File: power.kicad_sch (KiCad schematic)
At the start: 2 parts

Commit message: Updated power rails
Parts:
- added R39, R40: 0Ω, Resistor_SMD:R_0201_0603Metric, symbol Device:R_Small
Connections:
- new net +3.3V: R39.2
- new net +3.3VA: R40.2
- new net +3.3V_SYS: R39.1, R40.1

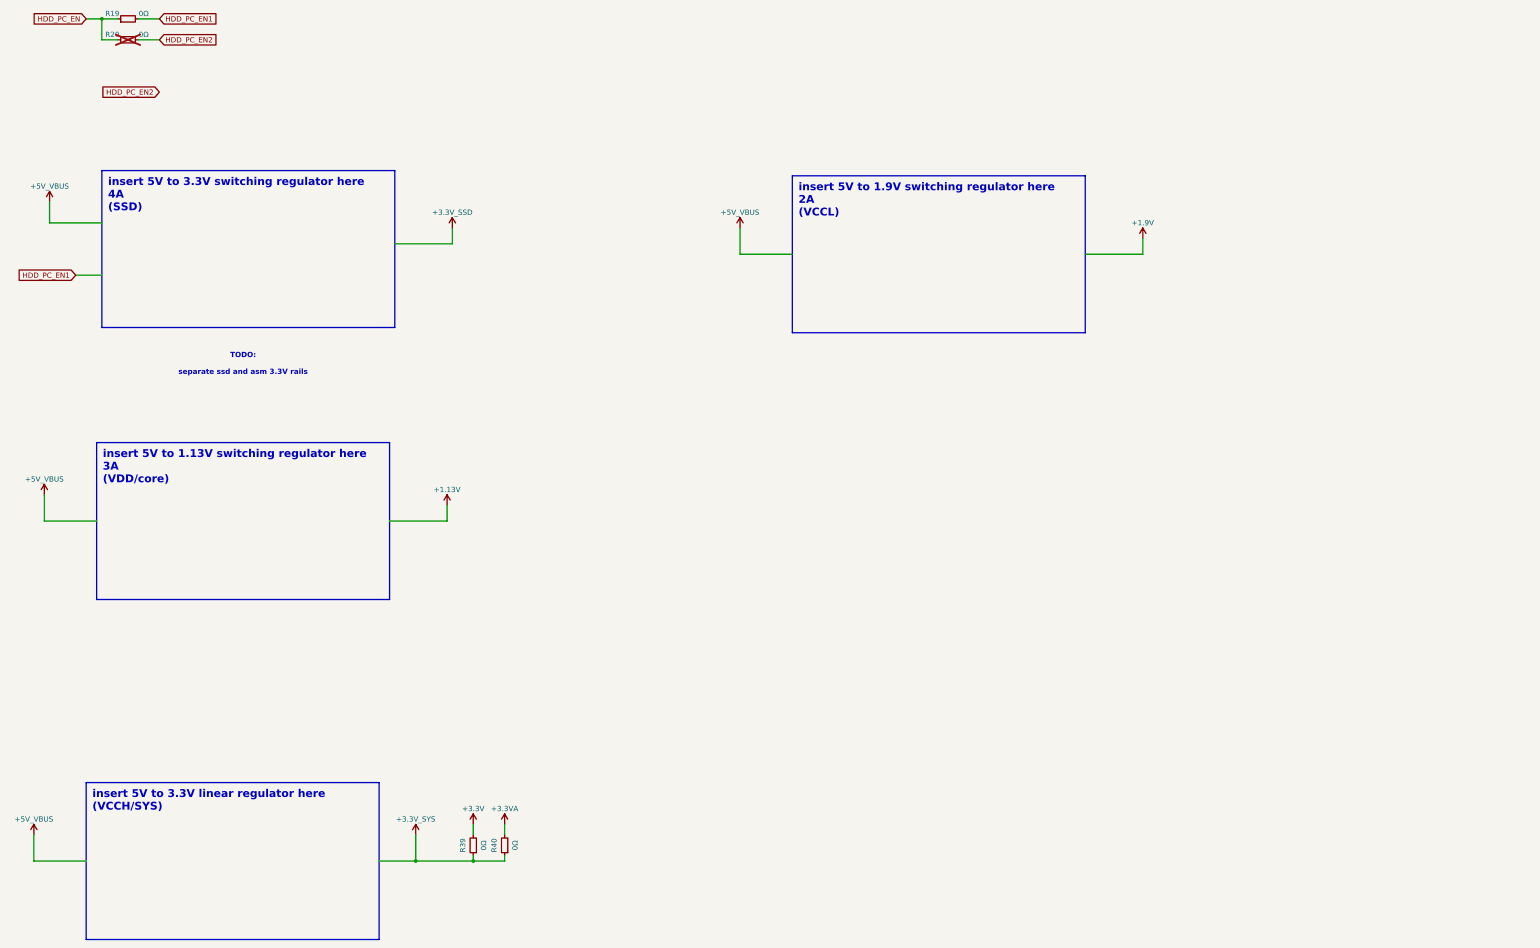
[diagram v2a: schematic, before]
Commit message: Changing from M.2 adapter to PCIe x4 adapter
I don't actually want an ssd enclosure, I want a PCIe-slot-giver for my laptop
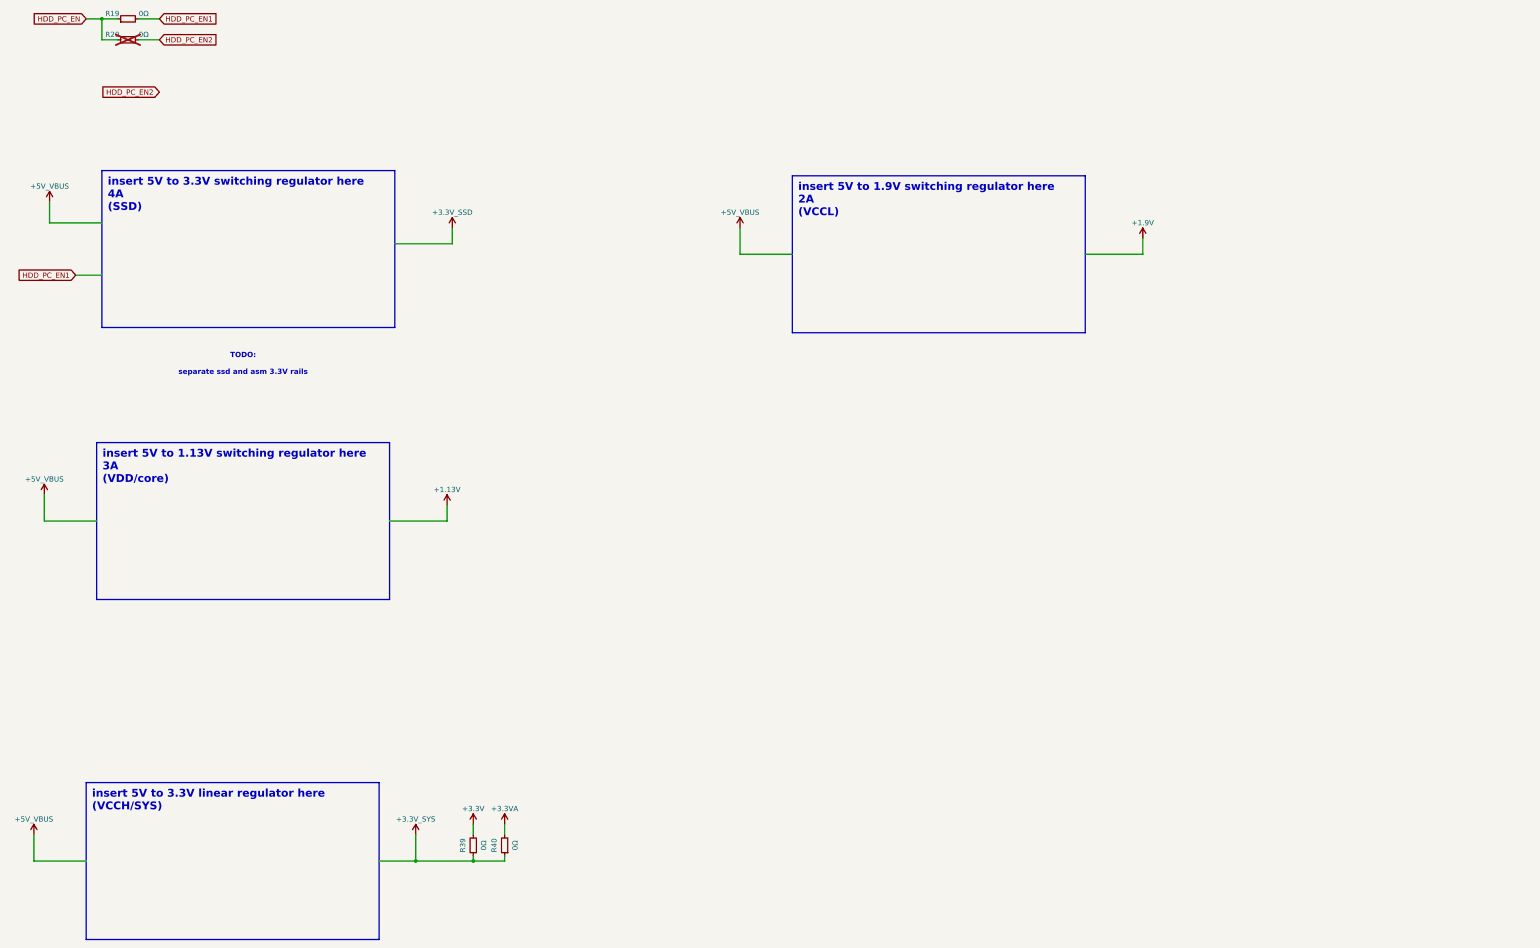
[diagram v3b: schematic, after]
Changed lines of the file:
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@@
 (kicad_sch
-	(version 20231120)
+	(version 20250114)
 	(generator "eeschema")
-	(generator_version "8.0")
+	(generator_version "9.0")
 	(paper "A3")
+	(text "TODO:\n\nseparate ssd and asm 3.3V rails"
+		(exclude_from_sim no)
+		(at 74.93 104.14 0)
+		(effects
+			(font
+				(size 1.27 1.27)
+				(thickness 0.254)
+				(bold yes)
+			)
+		)
+	)
+	(text_box "insert 5V to 1.13V switching regulator here\n3A\n(VDD/core)"
+		(exclude_from_sim no)
+		(at 39.37 123.19 0)
+		(size 71.12 38.1)
+		(margins 1.4288 1.4288 1.4288 1.4288)
+		(stroke
+			(width 0)
+			(type default)
+		)
+		(fill
+			(type none)
+		)
+		(effects
+			(font
+				(size 1.905 1.905)
+				(thickness 0.381)
+				(bold yes)
+			)
+			(justify left top)
+		)
+	)
+	(text_box "insert 5V to 1.9V switching regulator here\n2A\n(VCCL)"
+		(exclude_from_sim no)
+		(at 208.28 58.42 0)
+		(size 71.12 38.1)
+		(margins 1.4288 1.4288 1.4288 1.4288)
+		(stroke
+			(width 0)
+			(type default)
+		)
+		(fill
+			(type none)
+		)
+		(effects
+			(font
+				(size 1.905 1.905)
+				(thickness 0.381)
+				(bold yes)
+			)
+			(justify left top)
+		)
+	)
+	(text_box "insert 5V to 3.3V switching regulator here\n4A\n(SSD)\n"
+		(exclude_from_sim no)
+		(at 40.64 57.15 0)
+		(size 71.12 38.1)
+		(margins 1.4288 1.4288 1.4288 1.4288)
+		(stroke
+			(width 0)
+			(type default)
+		)
+		(fill
+			(type none)
+		)
+		(effects
+			(font
+				(size 1.905 1.905)
+				(thickness 0.381)
+				(bold yes)
+			)
+			(justify left top)
+		)
+	)
+	(text_box "insert 5V to 3.3V linear regulator here\n(VCCH/SYS)"
+		(exclude_from_sim no)
+		(at 36.83 205.74 0)
+		(size 71.12 38.1)
+		(margins 1.4288 1.4288 1.4288 1.4288)
+		(stroke
+			(width 0)
+			(type default)
+		)
+		(fill
+			(type none)
+		)
+		(effects
+			(font
+				(size 1.905 1.905)
+				(thickness 0.381)
+				(bold yes)
+			)
+			(justify left top)
+		)
+	)
 	(junction
 		(at 40.64 20.32)
@@
 		)
 	)
-	(text_box "insert 5V to 1.13V switching regulator here\n3A\n(VDD/core)"
-		(exclude_from_sim no)
-		(at 39.37 123.19 0)
-		(size 71.12 38.1)
-		(stroke
-			(width 0)
-			(type default)
-		)
-		(fill
-			(type none)
-		)
-		(effects
-			(font
-				(size 1.905 1.905)
-				(thickness 0.381)
-				(bold yes)
-			)
-			(justify left top)
-		)
-	)
-	(text_box "insert 5V to 1.9V switching regulator here\n2A\n(VCCL)"
-		(exclude_from_sim no)
-		(at 208.28 58.42 0)
-		(size 71.12 38.1)
-		(stroke
-			(width 0)
-			(type default)
-		)
-		(fill
-			(type none)
-		)
-		(effects
-			(font
-				(size 1.905 1.905)
-				(thickness 0.381)
-				(bold yes)
-			)
-			(justify left top)
-		)
-	)
-	(text_box "insert 5V to 3.3V switching regulator here\n4A\n(SSD)\n"
-		(exclude_from_sim no)
-		(at 40.64 57.15 0)
-		(size 71.12 38.1)
-		(stroke
-			(width 0)
-			(type default)
-		)
-		(fill
-			(type none)
-		)
-		(effects
-			(font
-				(size 1.905 1.905)
-				(thickness 0.381)
-				(bold yes)
-			)
-			(justify left top)
-		)
-	)
-	(text_box "insert 5V to 3.3V linear regulator here\n(VCCH/SYS)"
-		(exclude_from_sim no)
-		(at 36.83 205.74 0)
-		(size 71.12 38.1)
-		(stroke
-			(width 0)
-			(type default)
-		)
-		(fill
-			(type none)
-		)
-		(effects
-			(font
-				(size 1.905 1.905)
-				(thickness 0.381)
-				(bold yes)
-			)
-			(justify left top)
-		)
-	)
-	(text "TODO:\n\nseparate ssd and asm 3.3V rails"
-		(exclude_from_sim no)
-		(at 74.93 104.14 0)
-		(effects
-			(font
-				(size 1.27 1.27)
-				(thickness 0.254)
-				(bold yes)
-			)
-		)
-	)

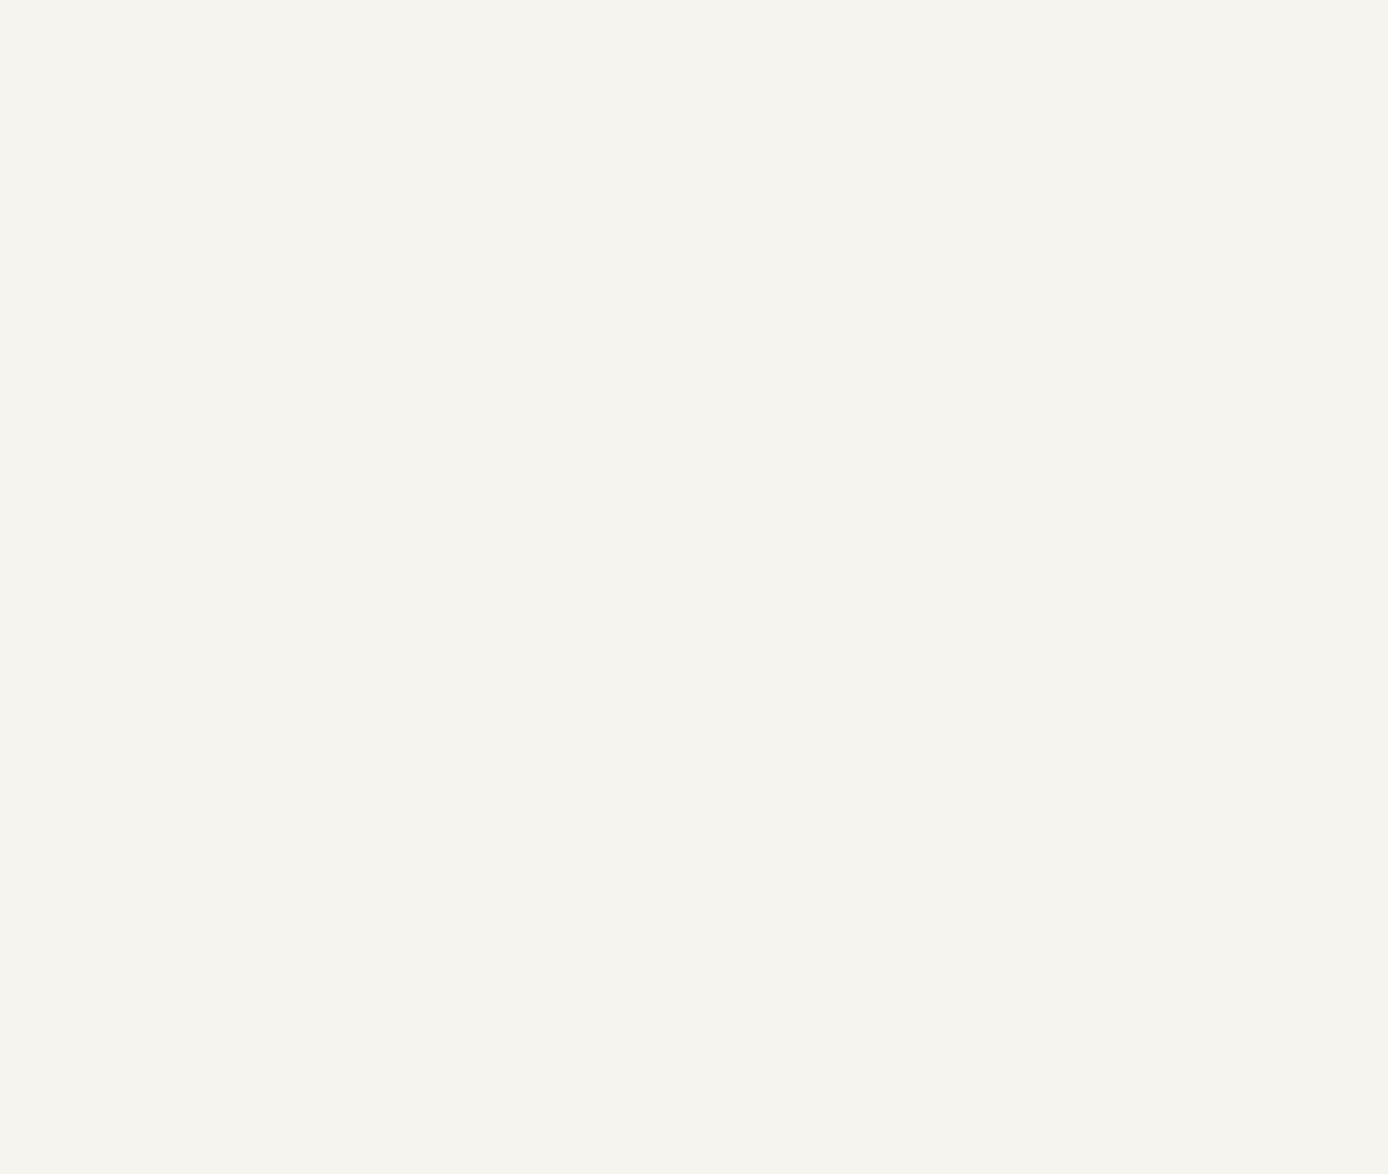
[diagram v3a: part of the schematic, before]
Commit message: Cleaning up schematic a bit
Directly copying the reference schematic was stupid lol, what a mess
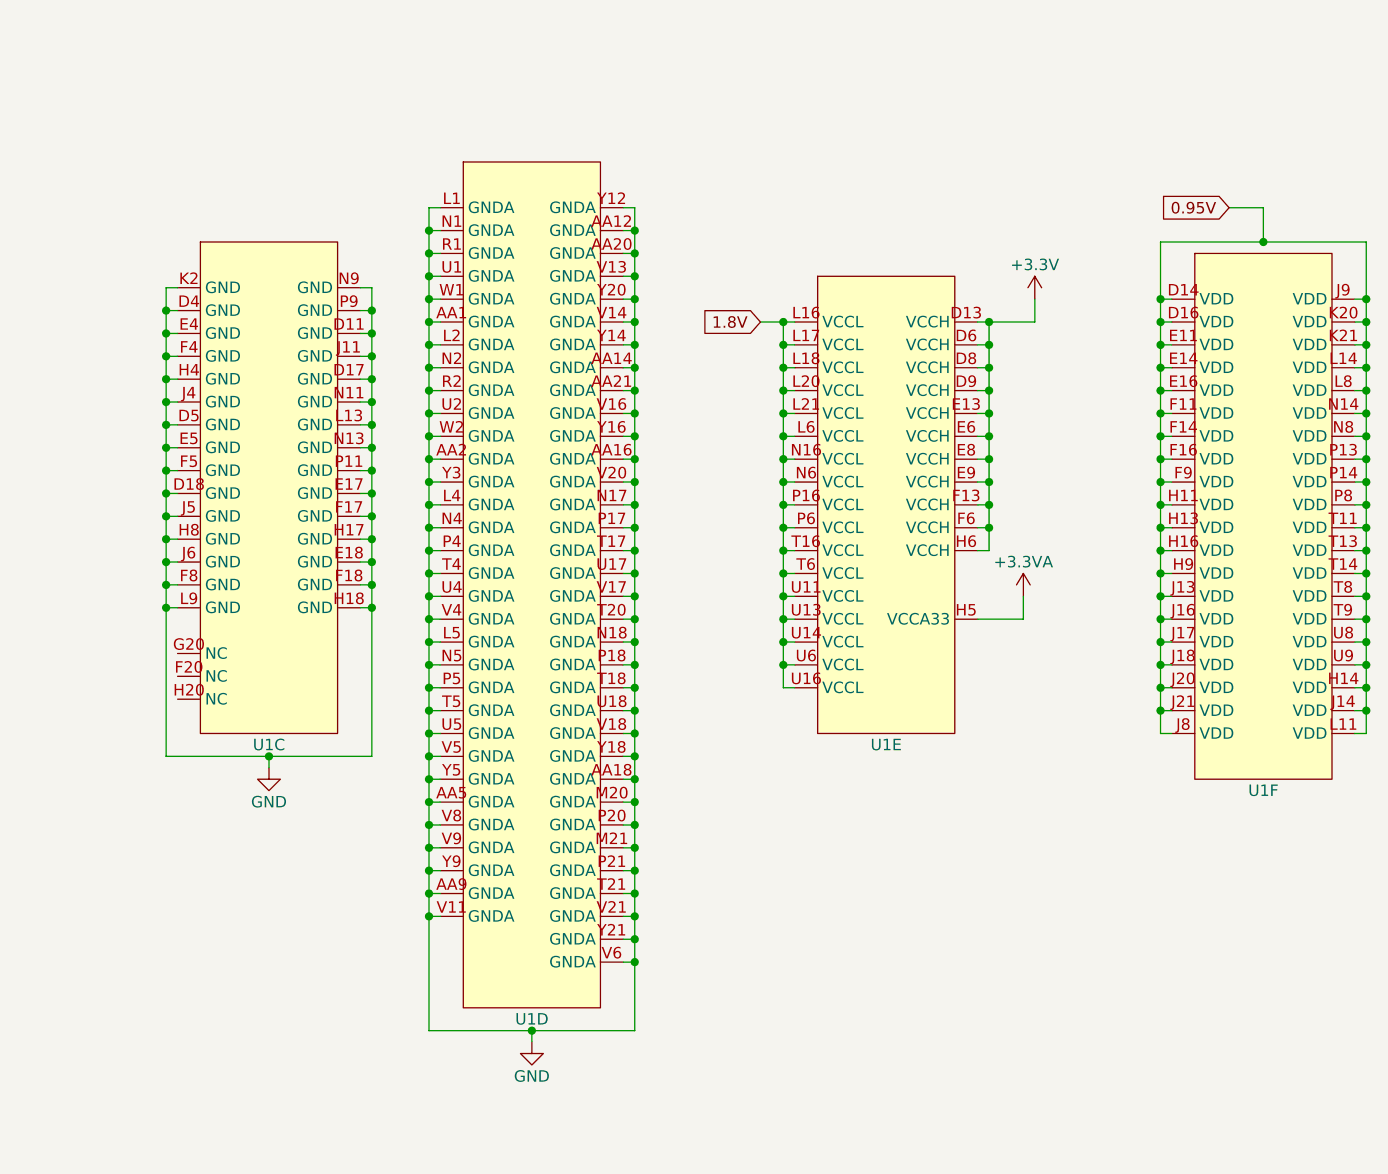
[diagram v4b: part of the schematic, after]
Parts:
- added U1: ~, A-my-stuff:ASM2464PD, symbol A_my_stuff:ASM2464PD
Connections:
- net +3.3V: now also U1.D13 (VCCH), U1.D6 (VCCH), U1.D8 (VCCH), U1.D9 (VCCH), U1.E13 (VCCH), U1.E6 (VCCH), U1.E8 (VCCH), U1.E9 (VCCH), U1.F13 (VCCH), U1.F6 (VCCH), U1.H6 (VCCH)
- net +3.3VA: now also U1.H5 (VCCA33)
- new net 0.95V: U1.D14 (VDD), U1.D16 (VDD), U1.E11 (VDD), U1.E14 (VDD), U1.E16 (VDD), U1.F11 (VDD), U1.F14 (VDD), U1.F16 (VDD), U1.F9 (VDD), U1.H11 (VDD), U1.H13 (VDD), U1.H14 (VDD), U1.H16 (VDD), U1.H9 (VDD), U1.J13 (VDD), U1.J14 (VDD), U1.J16 (VDD), U1.J17 (VDD), U1.J18 (VDD), U1.J20 (VDD), U1.J21 (VDD), U1.J8 (VDD), U1.J9 (VDD), U1.K20 (VDD), U1.K21 (VDD), U1.L11 (VDD), U1.L14 (VDD), U1.L8 (VDD), U1.N14 (VDD), U1.N8 (VDD), U1.P13 (VDD), U1.P14 (VDD), U1.P8 (VDD), U1.T11 (VDD), U1.T13 (VDD), U1.T14 (VDD), U1.T8 (VDD), U1.T9 (VDD), U1.U8 (VDD), U1.U9 (VDD)
- new net 1.8V: U1.L16 (VCCL), U1.L17 (VCCL), U1.L18 (VCCL), U1.L20 (VCCL), U1.L21 (VCCL), U1.L6 (VCCL), U1.N16 (VCCL), U1.N6 (VCCL), U1.P16 (VCCL), U1.P6 (VCCL), U1.T16 (VCCL), U1.T6 (VCCL), U1.U11 (VCCL), U1.U13 (VCCL), U1.U14 (VCCL), U1.U16 (VCCL), U1.U6 (VCCL)
- new net GND: U1.AA1 (GNDA), U1.AA12 (GNDA), U1.AA14 (GNDA), U1.AA16 (GNDA), U1.AA18 (GNDA), U1.AA2 (GNDA), U1.AA20 (GNDA), U1.AA21 (GNDA), U1.AA5 (GNDA), U1.AA9 (GNDA), U1.D11 (GND), U1.D17 (GND), U1.D18 (GND), U1.D4 (GND), U1.D5 (GND), U1.E17 (GND), U1.E18 (GND), U1.E4 (GND), U1.E5 (GND), U1.F17 (GND), U1.F18 (GND), U1.F4 (GND), U1.F5 (GND), U1.F8 (GND), U1.H17 (GND), U1.H18 (GND), U1.H4 (GND), U1.H8 (GND), U1.J11 (GND), U1.J4 (GND), U1.J5 (GND), U1.J6 (GND), U1.K2 (GND), U1.L1 (GNDA), U1.L13 (GND), U1.L2 (GNDA), U1.L4 (GNDA), U1.L5 (GNDA), U1.L9 (GND), U1.M20 (GNDA), U1.M21 (GNDA), U1.N1 (GNDA), U1.N11 (GND), U1.N13 (GND), U1.N17 (GNDA), U1.N18 (GNDA), U1.N2 (GNDA), U1.N4 (GNDA), U1.N5 (GNDA), U1.N9 (GND), U1.P11 (GND), U1.P17 (GNDA), U1.P18 (GNDA), U1.P20 (GNDA), U1.P21 (GNDA), U1.P4 (GNDA), U1.P5 (GNDA), U1.P9 (GND), U1.R1 (GNDA), U1.R2 (GNDA), U1.T17 (GNDA), U1.T18 (GNDA), U1.T20 (GNDA), U1.T21 (GNDA), U1.T4 (GNDA), U1.T5 (GNDA), U1.U1 (GNDA), U1.U17 (GNDA), U1.U18 (GNDA), U1.U2 (GNDA), U1.U4 (GNDA), U1.U5 (GNDA), U1.V11 (GNDA), U1.V13 (GNDA), U1.V14 (GNDA), U1.V16 (GNDA), U1.V17 (GNDA), U1.V18 (GNDA), U1.V20 (GNDA), U1.V21 (GNDA), U1.V4 (GNDA), U1.V5 (GNDA), U1.V6 (GNDA), U1.V8 (GNDA), U1.V9 (GNDA), U1.W1 (GNDA), U1.W2 (GNDA), U1.Y12 (GNDA), U1.Y14 (GNDA), U1.Y16 (GNDA), U1.Y18 (GNDA), U1.Y20 (GNDA), U1.Y21 (GNDA), U1.Y3 (GNDA), U1.Y5 (GNDA), U1.Y9 (GNDA)

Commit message: power notes
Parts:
- removed R20, R39: 0Ω, Resistor_SMD:R_0201_0603Metric, symbol Device:R_Small
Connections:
- net +3.3V_SYS is gone; now on net +3.3V_LDO: R40.1
- net +3.3V renamed +3.3V_LDO
- net 0.95V renamed VDD
- net 1.8V renamed VCCL
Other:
- company: (none) -> WifiCable
- title: (none) -> ASM2464PD power
- moved on the sheet: R19, R40, U1C, U1D, U1E, U1F

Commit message: Added function names to gpio pins
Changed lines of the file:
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@@
 		)
 	)
-	(text_box "insert 5V to 3.3V linear regulator here\n(VCCH/SYS)"
+	(text_box "insert 5V to 3.3V linear regulator here\n(1117 33)\n(VCCH/SYS)"
 		(exclude_from_sim no)
 		(at 36.83 205.74 0)
@@
 		(stroke
 			(width 0)
-			(type default)
+			(type solid)
 		)
 		(fill
@@
 		)
 		(instances
-			(project "ASM2464PD-test"
+			(project ""
+				(path "/b2a945ac-f788-482b-9831-47d865c602eb/12c26485-ec0e-483e-81eb-3c9eea5d2424"
+					(reference "U1")
+					(unit 5)
+				)
 				(path "/b2a945ac-f788-482b-9831-47d865c602eb/925879bc-4cbd-4ed0-8b1e-92f804aaa7cd"
 					(reference "U1")
@@
 		)
 		(instances
-			(project "ASM2464PD-test"
+			(project ""
+				(path "/b2a945ac-f788-482b-9831-47d865c602eb/12c26485-ec0e-483e-81eb-3c9eea5d2424"
+					(reference "U1")
+					(unit 4)
+				)
 				(path "/b2a945ac-f788-482b-9831-47d865c602eb/925879bc-4cbd-4ed0-8b1e-92f804aaa7cd"
 					(reference "U1")
@@
 		)
 		(instances
-			(project "ASM2464PD-test"
+			(project ""
+				(path "/b2a945ac-f788-482b-9831-47d865c602eb/12c26485-ec0e-483e-81eb-3c9eea5d2424"
+					(reference "U1")
+					(unit 3)
+				)
 				(path "/b2a945ac-f788-482b-9831-47d865c602eb/925879bc-4cbd-4ed0-8b1e-92f804aaa7cd"
 					(reference "U1")
@@
 		)
 		(instances
-			(project "ASM2464PD-test"
+			(project ""
+				(path "/b2a945ac-f788-482b-9831-47d865c602eb/12c26485-ec0e-483e-81eb-3c9eea5d2424"
+					(reference "U1")
+					(unit 6)
+				)
 				(path "/b2a945ac-f788-482b-9831-47d865c602eb/925879bc-4cbd-4ed0-8b1e-92f804aaa7cd"
 					(reference "U1")

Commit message: more pin names, more schematic cleanup, added SPI header
baby I don't know when I'm supposed to stop (I should go to bed)
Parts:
- R19, R40: footprint Resistor_SMD:R_0201_0603Metric -> Resistor_SMD:R_0402_1005Metric
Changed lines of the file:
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@@
 			)
 		)
-		(property "Footprint" "Resistor_SMD:R_0201_0603Metric"
+		(property "Footprint" "Resistor_SMD:R_0402_1005Metric"
 			(at 68.58 46.99 0)
 			(effects
@@
 			)
 		)
-		(property "Footprint" "Resistor_SMD:R_0201_0603Metric"
+		(property "Footprint" "Resistor_SMD:R_0402_1005Metric"
 			(at 134.62 220.98 0)
 			(effects

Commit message: component arrangement
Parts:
- removed R19: 0Ω, Resistor_SMD:R_0402_1005Metric, symbol Device:R_Small
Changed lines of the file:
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@@
 	(wire
 		(pts
-			(xy 58.42 46.99) (xy 66.04 46.99)
-		)
-		(stroke
-			(width 0)
-			(type default)
-		)
-	)
-	(wire
-		(pts
 			(xy 386.08 208.28) (xy 387.35 208.28)
 		)
@@
 	(wire
 		(pts
-			(xy 71.12 46.99) (xy 76.2 46.99)
-		)
-		(stroke
-			(width 0)
-			(type default)
-		)
-	)
-	(wire
-		(pts
 			(xy 387.35 152.4) (xy 387.35 154.94)
 		)
@@
 		)
 	)
-	(global_label "HDD_PC_EN1"
-		(shape input)
-		(at 76.2 46.99 0)
-		(fields_autoplaced yes)
-		(effects
-			(font
-				(size 1.27 1.27)
-			)
-			(justify left)
-		)
-		(property "Intersheetrefs" "${INTERSHEET_REFS}"
-			(at 91.2199 46.99 0)
-			(effects
-				(font
-					(size 1.27 1.27)
-				)
-				(justify left)
-				(hide yes)
-			)
-		)
-	)
-	(global_label "HDD_PC_EN1"
-		(shape input)
-		(at 34.29 82.55 180)
-		(fields_autoplaced yes)
-		(effects
-			(font
-				(size 1.27 1.27)
-			)
-			(justify right)
-		)
-		(property "Intersheetrefs" "${INTERSHEET_REFS}"
-			(at 19.2701 82.55 0)
-			(effects
-				(font
-					(size 1.27 1.27)
-				)
-				(justify right)
-				(hide yes)
-			)
-		)
-	)
 	(global_label "HDD_PC_EN"
 		(shape input)
-		(at 58.42 46.99 180)
+		(at 34.29 82.55 180)
 		(fields_autoplaced yes)
 		(effects
@@
 		)
 		(property "Intersheetrefs" "${INTERSHEET_REFS}"
-			(at 44.6096 46.99 0)
+			(at 20.4796 82.55 0)
 			(effects
 				(font
@@
 					(unit 1)
 				)
-			)
-		)
-	)
-	(symbol
-		(lib_id "Device:R_Small")
-		(at 68.58 46.99 90)
-		(unit 1)
-		(exclude_from_sim no)
-		(in_bom yes)
-		(on_board yes)
-		(dnp no)
-		(property "Reference" "R19"
-			(at 64.77 45.72 90)
-			(effects
-				(font
-					(size 1.27 1.27)
-				)
-			)
-		)
-		(property "Value" "0Ω"
-			(at 72.39 45.72 90)
-			(effects
-				(font
-					(size 1.27 1.27)
-				)
-			)
-		)
-		(property "Footprint" "Resistor_SMD:R_0402_1005Metric"
-			(at 68.58 46.99 0)
-			(effects
-				(font
-					(size 1.27 1.27)
-				)
-				(hide yes)
-			)
-		)
-		(property "Datasheet" "~"
-			(at 68.58 46.99 0)
-			(effects
-				(font
-					(size 1.27 1.27)
-				)
-				(hide yes)
-			)
-		)
-		(property "Description" "Resistor, small symbol"
-			(at 68.58 46.99 0)
-			(effects
-				(font
-					(size 1.27 1.27)
-				)
-				(hide yes)
-			)
-		)
-		(pin "1"
-		)
-		(pin "2"
-		)
-		(instances
-			(project "ASM2464PD-test"
-				(path "/b2a945ac-f788-482b-9831-47d865c602eb/925879bc-4cbd-4ed0-8b1e-92f804aaa7cd"
-					(reference "R19")
-					(unit 1)
-				)
